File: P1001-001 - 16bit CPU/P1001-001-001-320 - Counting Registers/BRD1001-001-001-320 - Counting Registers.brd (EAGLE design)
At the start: 200 x 48 mm, 15 parts, among them IC1 74HC192D, IC12 74AC245DW, IC2 74HC192D, IC27 MEGA8535-A, IC3 74HC192D, IC4 74HC192D, IC7 74AC245DW, J1 22-27-2041-04

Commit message: Finished All Boards
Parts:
- added C1, C2, C3, C4: 1uF, rcl:C1206
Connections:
- net GND: now also C1.2, C2.2, C3.2, C4.2
- net VCC: now also C1.1, C2.1, C3.1, C4.1
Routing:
- net VCC: track 240.9 -> 373.3 mm, vias 15 -> 17
- net GND: track 324.2 -> 411.2 mm, vias 13 -> 16

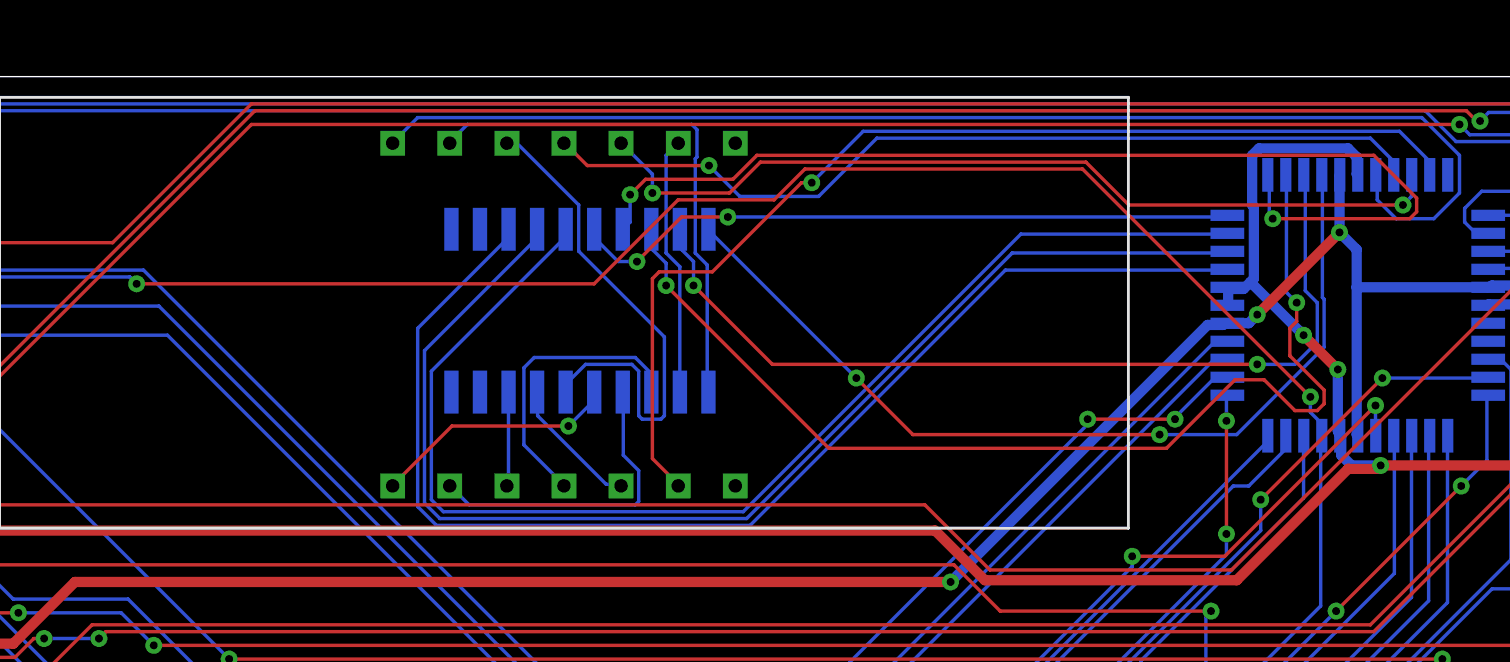
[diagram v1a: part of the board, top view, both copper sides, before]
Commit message: fix the 16 register problem
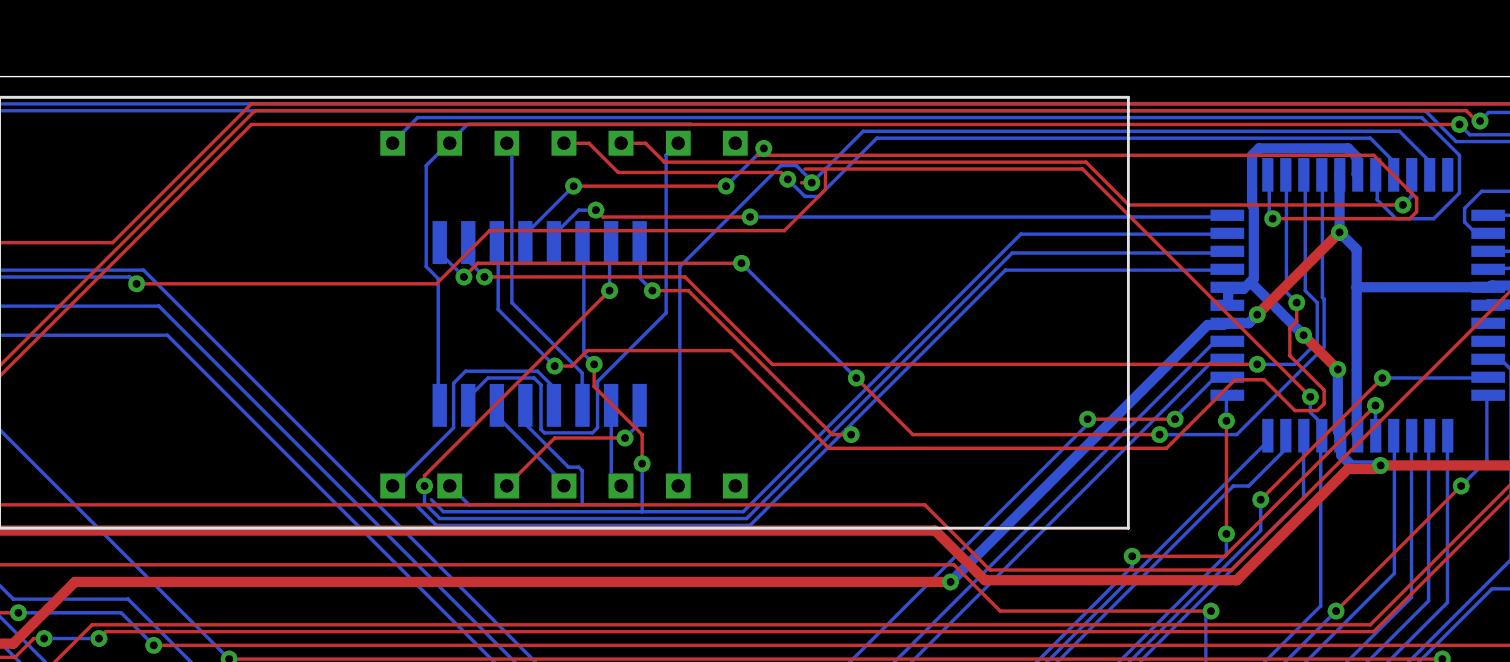
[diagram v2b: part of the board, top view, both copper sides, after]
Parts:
- removed RN2: (no value), resistor-dil:SOMC20
- added RN1: (no value), resistor-dil:SOMC16
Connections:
- net A: now also RN1.9; no longer RN2.20
- net B: now also RN1.10; no longer RN2.19
- net C: now also RN1.11; no longer RN2.18
- net D: now also RN1.12; no longer RN2.17
- net DP: now also RN1.16; no longer RN2.13
- net E: now also RN1.13; no longer RN2.16
- net F: now also RN1.14; no longer RN2.15
- net G: now also RN1.15; no longer RN2.14
- net N$24: now also RN1.8; no longer RN2.1
- net N$25: now also RN1.7; no longer RN2.2
- net N$26: now also RN1.6; no longer RN2.3
- net N$27: now also RN1.5; no longer RN2.4
- net N$28: now also RN1.4; no longer RN2.5
- net N$29: now also RN1.3; no longer RN2.6
- net N$30: now also RN1.2; no longer RN2.7
- net N$31: now also RN1.1; no longer RN2.8
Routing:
- net A: track 40.5 -> 53.0 mm, vias 2 -> 4
- net N$25: track 11.5 -> 23.6 mm
- net N$29: track 22.6 -> 13.6 mm
- net B: track 40.0 -> 48.6 mm
- net N$26: track 13.0 -> 4.91 mm
- net C: track 48.1 -> 56.0 mm
- net D: track 47.4 -> 52.2 mm, vias 2 -> 4
- net N$31: track 4.20 -> 7.98 mm, vias 0 -> 1
- net N$30: track 6.06 -> 3.76 mm
- net DIG2: track 39.0 -> 37.4 mm, vias 2 -> 1
- net SIGNAL8: track 172.4 -> 173.9 mm
- net F: track 55.2 -> 53.8 mm, vias 0 -> 2
- net E: track 29.8 -> 31.0 mm
- net G: track 55.2 -> 56.0 mm, vias 0 -> 2
- net N$28: track 10.9 -> 11.5 mm, vias 1 -> 0
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
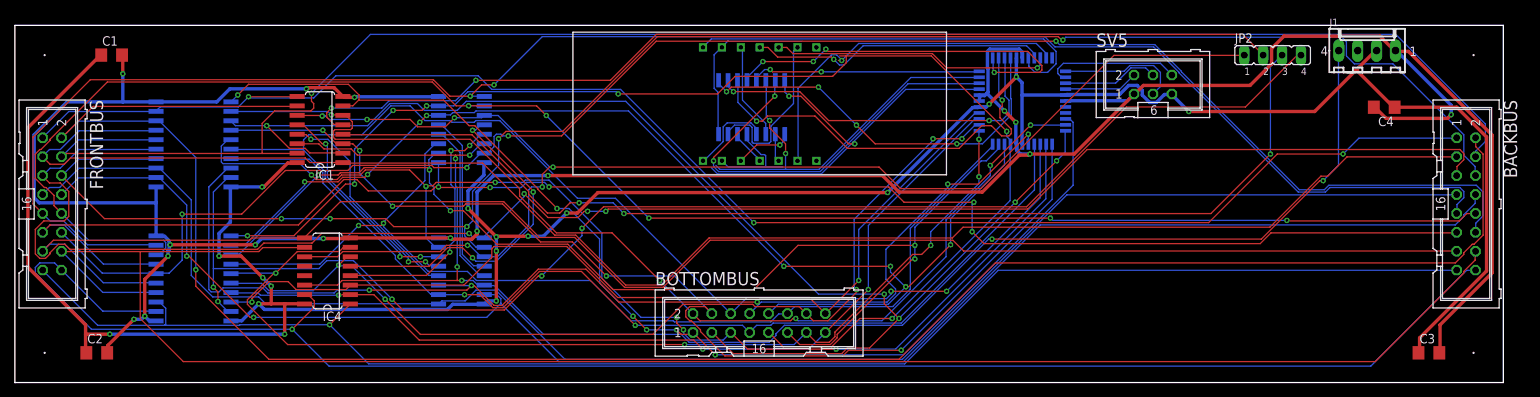
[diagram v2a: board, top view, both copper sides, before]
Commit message: Fix problems with registers
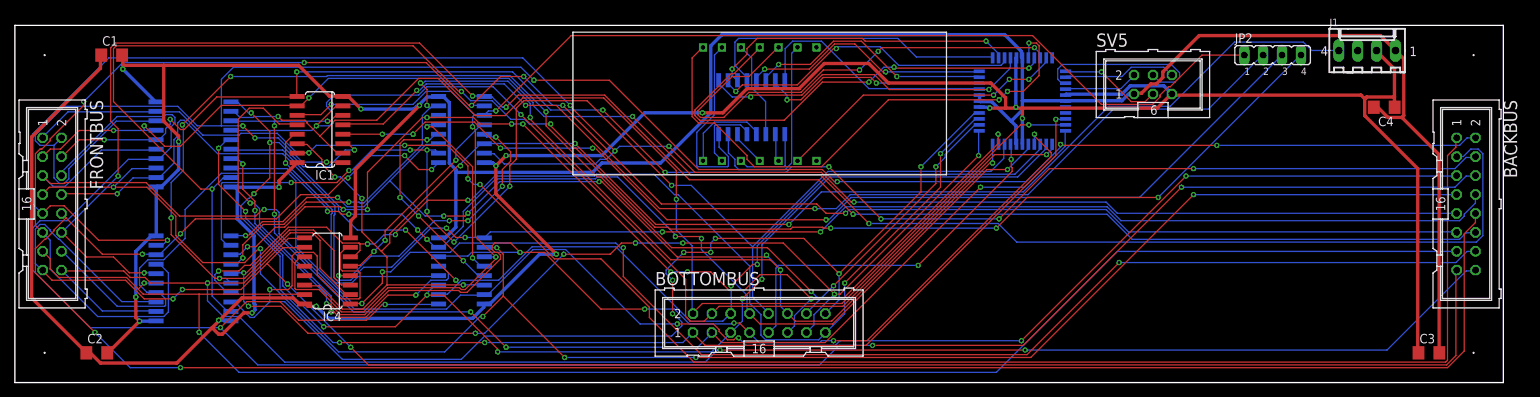
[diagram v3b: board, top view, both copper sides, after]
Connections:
- net BUS0: now also IC1.15; no longer IC1.9
- net BUS1: now also IC1.1; no longer IC1.10
- net BUS10: now also IC3.10; no longer IC3.1
- net BUS11: now also IC3.9; no longer IC3.15
- net BUS12: now also IC4.15; no longer IC4.9
- net BUS13: now also IC4.1; no longer IC4.10
- net BUS14: now also IC4.10; no longer IC4.1
- net BUS15: now also IC4.9; no longer IC4.15
- net BUS2: now also IC1.10; no longer IC1.1
- net BUS3: now also IC1.9; no longer IC1.15
- net BUS4: now also IC2.15; no longer IC2.9
- net BUS5: now also IC2.1; no longer IC2.10
- net BUS6: now also IC2.10; no longer IC2.1
- net BUS7: now also IC2.9; no longer IC2.15
- net BUS8: now also IC3.15; no longer IC3.9
- net BUS9: now also IC3.1; no longer IC3.10
- net SIGNAL0: now also IC1.3; no longer IC1.7
- net SIGNAL1: now also IC1.2; no longer IC1.6
- net SIGNAL10: now also IC3.6; no longer IC3.2
- net SIGNAL11: now also IC3.7; no longer IC3.3
- net SIGNAL12: now also IC4.3; no longer IC4.7
- net SIGNAL13: now also IC4.2; no longer IC4.6
- net SIGNAL14: now also IC4.6; no longer IC4.2
- net SIGNAL15: now also IC4.7; no longer IC4.3
- net SIGNAL2: now also IC1.6; no longer IC1.2
- net SIGNAL3: now also IC1.7; no longer IC1.3
- net SIGNAL4: now also IC2.3; no longer IC2.7
- net SIGNAL5: now also IC2.2; no longer IC2.6
- net SIGNAL6: now also IC2.6; no longer IC2.2
- net SIGNAL7: now also IC2.7; no longer IC2.3
- net SIGNAL8: now also IC3.3; no longer IC3.7
- net SIGNAL9: now also IC3.2; no longer IC3.6
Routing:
- net SIGNAL13: track 128.2 -> 189.2 mm, vias 5 -> 8
- net BUS5: track 237.6 -> 294.4 mm, vias 5 -> 4
- net GND: track 411.2 -> 356.5 mm, vias 16 -> 6
- net BUS9: track 235.5 -> 286.1 mm, vias 5 -> 7
- net SIGNAL15: track 124.4 -> 171.7 mm, vias 2 -> 8
- net !REG_OUT: track 184.5 -> 226.1 mm, vias 5 -> 6
- net BUS14: track 208.4 -> 244.0 mm, vias 1 -> 4
- net BUS10: track 221.9 -> 253.8 mm, vias 5 -> 6
- net N$2: track 29.7 -> 61.5 mm
- net SIGNAL8: track 173.9 -> 145.0 mm, vias 7 -> 8
- net DIG2: track 37.4 -> 65.9 mm, vias 1 -> 3
- net BUS0: track 213.2 -> 239.3 mm, vias 3 -> 4
- net SIGNAL6: track 136.9 -> 162.8 mm, vias 2 -> 8
- net SIGNAL14: track 121.7 -> 147.6 mm, vias 3 -> 6
- net G: track 56.0 -> 30.6 mm
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
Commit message: Check in the first try at soldering up the board
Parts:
- moved C3 6.00 mm to (184.0, 4.00)
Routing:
- net SIGNAL5: track 140.0 -> 229.4 mm, vias 4 -> 5
- net SIGNAL11: track 149.8 -> 237.3 mm, vias 7 -> 8
- net SIGNAL4: track 152.9 -> 236.4 mm, vias 7 -> 6
- net SIGNAL12: track 153.7 -> 228.6 mm
- net SIGNAL2: track 157.4 -> 229.0 mm
- net BUS5: track 294.4 -> 224.4 mm
- net VCC: track 381.7 -> 444.0 mm, vias 11 -> 14
- net CLEAR: track 202.6 -> 253.3 mm, vias 6 -> 9
- net GND: track 356.5 -> 406.7 mm, vias 6 -> 21
- net SIGNAL13: track 189.2 -> 140.2 mm, vias 8 -> 10
- net !REG_IN: track 200.0 -> 244.2 mm, vias 4 -> 5
- net BUS14: track 244.0 -> 286.6 mm
- net DIG0: track 72.2 -> 114.3 mm, vias 3 -> 4
- net SIGNAL1: track 156.6 -> 196.6 mm, vias 3 -> 9
- net N$3: track 38.1 -> 78.0 mm, vias 1 -> 5
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
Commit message: Add the prototype stuff
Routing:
- net SIGNAL4: track 236.4 -> 141.4 mm, vias 6 -> 10
- net SIGNAL12: track 228.6 -> 156.8 mm, vias 8 -> 7
- net VCC: track 444.0 -> 379.0 mm, vias 14 -> 8
- net SIGNAL2: track 229.0 -> 165.5 mm, vias 6 -> 4
- net SIGNAL11: track 237.3 -> 175.7 mm, vias 8 -> 9
- net SIGNAL5: track 229.4 -> 171.7 mm, vias 5 -> 11
- net GND: track 406.7 -> 350.2 mm, vias 21 -> 5
- net CLEAR: track 253.3 -> 207.4 mm, vias 9 -> 4
- net BUS1: track 246.4 -> 291.8 mm, vias 4 -> 5
- net BUS12: track 233.4 -> 278.4 mm
- net !REG_IN: track 244.2 -> 200.4 mm, vias 5 -> 3
- net SIGNAL10: track 171.2 -> 214.8 mm
- net SIGNAL15: track 143.8 -> 187.5 mm, vias 8 -> 7
- net SIGNAL1: track 196.6 -> 153.4 mm, vias 9 -> 5
- net BUS5: track 224.4 -> 266.0 mm, vias 4 -> 5
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
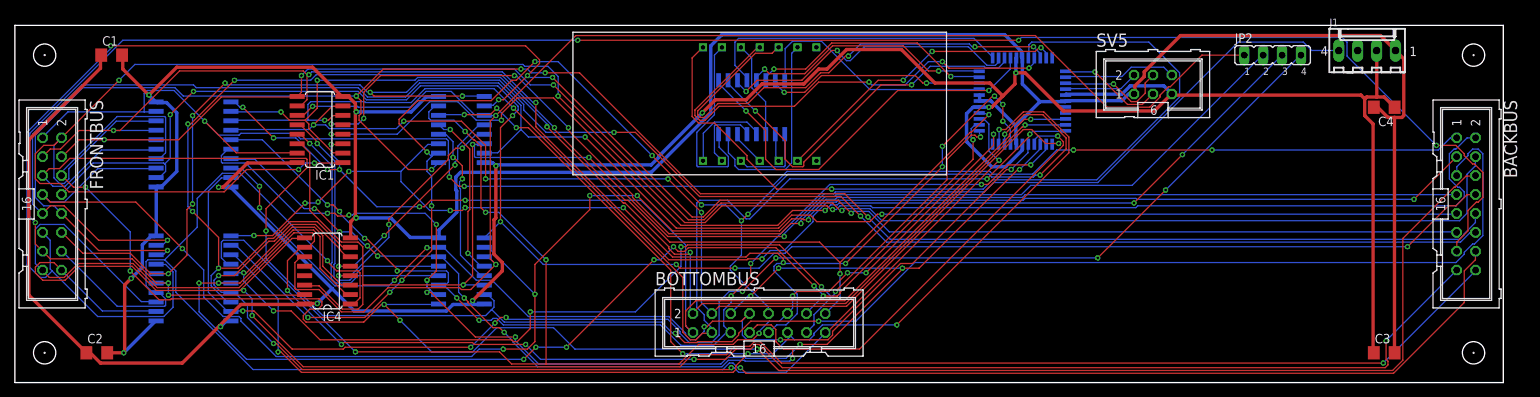
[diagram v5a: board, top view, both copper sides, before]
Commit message: add ram to Memory
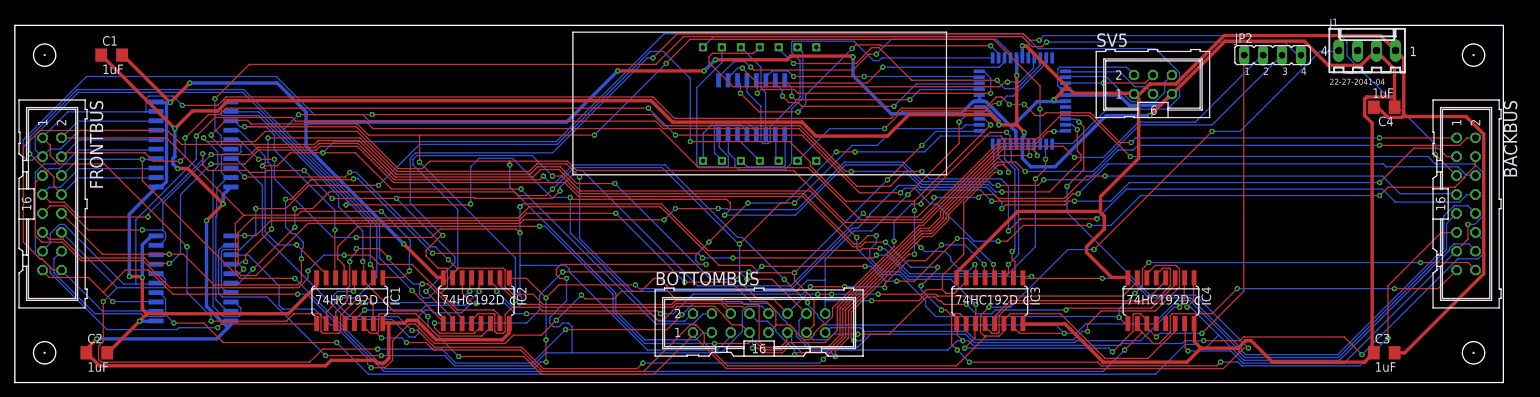
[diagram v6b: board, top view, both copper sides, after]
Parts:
- moved IC4 112.1 mm to (154.0, 11.0), turned to 180 degrees
- moved IC3 74.6 mm to (131.0, 11.0), flipped to the top, turned to 180 degrees
- moved IC1 23.3 mm to (45.0, 11.0), turned to 180 degrees
- moved IC2 4.47 mm to (62.0, 11.0), flipped to the top, turned to 180 degrees
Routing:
- net SIGNAL3: track 149.6 -> 245.7 mm, vias 6 -> 4
- net GND: track 350.2 -> 432.0 mm, vias 5 -> 12
- net BUS2: track 224.5 -> 306.3 mm, vias 5 -> 6
- net SIGNAL14: track 154.5 -> 227.8 mm, vias 4 -> 8
- net VCC: track 379.0 -> 450.5 mm, vias 8 -> 9
- net N$5: track 22.8 -> 93.9 mm, vias 2 -> 8
- net DIG0: track 112.0 -> 46.8 mm, vias 1 -> 0
- net SIGNAL0: track 152.7 -> 213.6 mm, vias 8 -> 6
- net N$4: track 22.6 -> 82.4 mm, vias 2 -> 6
- net BUS3: track 221.0 -> 280.3 mm, vias 4 -> 9
- net SIGNAL10: track 214.8 -> 162.7 mm, vias 8 -> 7
- net SIGNAL4: track 141.4 -> 190.2 mm, vias 10 -> 9
- net BUS0: track 221.3 -> 269.9 mm, vias 5 -> 7
- net BUS13: track 266.0 -> 225.1 mm, vias 2 -> 3
- net BUS7: track 233.0 -> 273.2 mm, vias 7 -> 6
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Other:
- board text added: "BRD1001-001-001-320 A Counting Registers"
- board text added: "Copyright 2020 James Wright"
